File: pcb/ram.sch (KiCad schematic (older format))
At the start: 12 parts, among them J1 CONN_INTEGRALSTICK_FPGA_DEVICE, U2 XC7A50T-1FTG256C, U3 S27KS0641, U4 S27KS0641

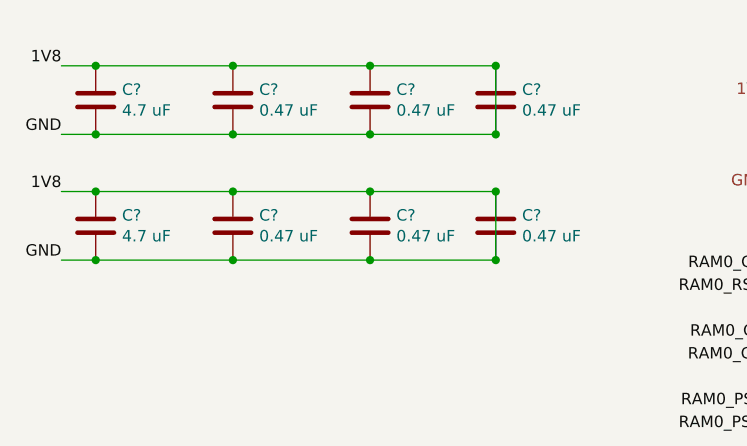
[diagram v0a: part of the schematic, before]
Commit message: Finished initial schematic. Pin assignments will likely change during routing. Ready for test point insertion and signoff review.
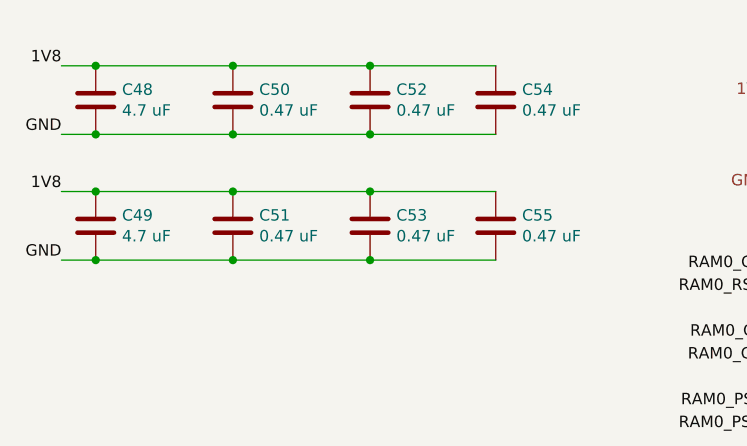
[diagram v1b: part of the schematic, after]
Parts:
- gave numbers to parts that had none: 8
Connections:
- net 1V8: no longer C48.2, C49.2, C50.2, C51.2, C52.2, C53.2, C54.2, C55.2, U3.B3 (VSS), U3.C1 (VSSQ), U3.E5 (VSSQ), U4.B3 (VSS), U4.C1 (VSSQ), U4.E5 (VSSQ)
- new net GND: C48.2, C49.2, C50.2, C51.2, C52.2, C53.2, C54.2, C55.2, U3.B3 (VSS), U3.C1 (VSSQ), U3.E5 (VSSQ), U4.B3 (VSS), U4.C1 (VSSQ), U4.E5 (VSSQ)
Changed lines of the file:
@@
 $Descr A4 11693 8268
 encoding utf-8
-Sheet 6 7
+Sheet 7 8
 Title "INTEGRALSTICK Compute Module"
-Date "2018-11-06"
+Date "2018-11-07"
 Rev "0.1"
 Comp "Andrew D. Zonenberg"
-Comment1 ""
+Comment1 "HyperRAM and 1.8V GPIO"
 Comment2 ""
 Comment3 ""
@@
 CLK_1V8_1
 $Comp
-L device:C C?
+L device:C C48
 U 1 1 5BF7E63E
 P 1000 950
-F 0 "C?" H 1115 996 50  0000 L CNN
+F 0 "C48" H 1115 996 50  0000 L CNN
 F 1 "4.7 uF" H 1115 905 50  0000 L CNN
 F 2 "" H 1038 800 50  0001 C CNN
@@
 $EndComp
 $Comp
-L device:C C?
+L device:C C50
 U 1 1 5BF7F429
 P 1600 950
-F 0 "C?" H 1715 996 50  0000 L CNN
+F 0 "C50" H 1715 996 50  0000 L CNN
 F 1 "0.47 uF" H 1715 905 50  0000 L CNN
 F 2 "" H 1638 800 50  0001 C CNN
@@
 $EndComp
 $Comp
-L device:C C?
+L device:C C52
 U 1 1 5BF7F82E
 P 2200 950
-F 0 "C?" H 2315 996 50  0000 L CNN
+F 0 "C52" H 2315 996 50  0000 L CNN
 F 1 "0.47 uF" H 2315 905 50  0000 L CNN
 F 2 "" H 2238 800 50  0001 C CNN
@@
 $EndComp
 $Comp
-L device:C C?
+L device:C C54
 U 1 1 5BF7FC5D
 P 2750 950
-F 0 "C?" H 2865 996 50  0000 L CNN
+F 0 "C54" H 2865 996 50  0000 L CNN
 F 1 "0.47 uF" H 2865 905 50  0000 L CNN
 F 2 "" H 2788 800 50  0001 C CNN
@@
 Wire Wire Line
 	850  1100 1000 1100
-Wire Wire Line
-	2750 1100 2750 800
-Connection ~ 2750 1100
 Connection ~ 1000 1100
 Wire Wire Line
@@
 Wire Wire Line
 	850  800  1000 800
-Connection ~ 2750 800
 Connection ~ 1000 800
 Wire Wire Line
@@
 	2200 800  2750 800
 $Comp
-L device:C C?
+L device:C C49
 U 1 1 5BF87471
 P 1000 1500
-F 0 "C?" H 1115 1546 50  0000 L CNN
+F 0 "C49" H 1115 1546 50  0000 L CNN
 F 1 "4.7 uF" H 1115 1455 50  0000 L CNN
 F 2 "" H 1038 1350 50  0001 C CNN
@@
 $EndComp
 $Comp
-L device:C C?
+L device:C C51
 U 1 1 5BF8747B
 P 1600 1500
-F 0 "C?" H 1715 1546 50  0000 L CNN
+F 0 "C51" H 1715 1546 50  0000 L CNN
 F 1 "0.47 uF" H 1715 1455 50  0000 L CNN
 F 2 "" H 1638 1350 50  0001 C CNN
@@
 $EndComp
 $Comp
-L device:C C?
+L device:C C53
 U 1 1 5BF87485
 P 2200 1500
-F 0 "C?" H 2315 1546 50  0000 L CNN
+F 0 "C53" H 2315 1546 50  0000 L CNN
 F 1 "0.47 uF" H 2315 1455 50  0000 L CNN
 F 2 "" H 2238 1350 50  0001 C CNN
@@
 $EndComp
 $Comp
-L device:C C?
+L device:C C55
 U 1 1 5BF8748F
 P 2750 1500
-F 0 "C?" H 2865 1546 50  0000 L CNN
+F 0 "C55" H 2865 1546 50  0000 L CNN
 F 1 "0.47 uF" H 2865 1455 50  0000 L CNN
 F 2 "" H 2788 1350 50  0001 C CNN
@@
 Wire Wire Line
 	850  1650 1000 1650
-Wire Wire Line
-	2750 1650 2750 1350
-Connection ~ 2750 1650
 Connection ~ 1000 1650
 Wire Wire Line
@@
 Wire Wire Line
 	850  1350 1000 1350
-Connection ~ 2750 1350
 Connection ~ 1000 1350
 Wire Wire Line

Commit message: Finished schematic signoff review. Fixed oscillator pinout bug, added some test points.
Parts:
- added TP11, TP12, TP13, TP14, TP15, TP16: SOLDERPROBE, symbol conn:CONN_01X01
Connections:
- net RAM0_CK_N: now also TP12.1 (P1)
- net RAM0_CK_P: now also TP11.1 (P1)
- net RAM0_DQ0: now also TP16.1 (P1)
- net RAM0_DQS: now also TP15.1 (P1)
- net RAM0_PSC_N: now also TP14.1 (P1)
- net RAM0_PSC_P: now also TP13.1 (P1)
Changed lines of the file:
@@
 Sheet 7 8
 Title "INTEGRALSTICK Compute Module"
-Date "2018-11-07"
+Date "2018-11-09"
 Rev "0.1"
 Comp "Andrew D. Zonenberg"
@@
 Wire Wire Line
 	2200 1350 2750 1350
+$Comp
+L conn:CONN_01X01 TP11
+U 1 1 5D407FEC
+P 1850 2350
+F 0 "TP11" H 1928 2391 50  0000 L CNN
+F 1 "SOLDERPROBE" H 1928 2300 50  0000 L CNN
+F 2 "" H 1850 2350 50  0001 C CNN
+F 3 "" H 1850 2350 50  0001 C CNN
+	1    1850 2350
+	1    0    0    -1
+$EndComp
+Text Label 1650 2350 2    50   ~ 0
+RAM0_CK_P
+$Comp
+L conn:CONN_01X01 TP12
+U 1 1 5D408C8E
+P 1850 2600
+F 0 "TP12" H 1928 2641 50  0000 L CNN
+F 1 "SOLDERPROBE" H 1928 2550 50  0000 L CNN
+F 2 "" H 1850 2600 50  0001 C CNN
+F 3 "" H 1850 2600 50  0001 C CNN
+	1    1850 2600
+	1    0    0    -1
+$EndComp
+Text Label 1650 2600 2    50   ~ 0
+RAM0_CK_N
+$Comp
+L conn:CONN_01X01 TP13
+U 1 1 5D40CFAA
+P 1850 2900
+F 0 "TP13" H 1928 2941 50  0000 L CNN
+F 1 "SOLDERPROBE" H 1928 2850 50  0000 L CNN
+F 2 "" H 1850 2900 50  0001 C CNN
+F 3 "" H 1850 2900 50  0001 C CNN
+	1    1850 2900
+	1    0    0    -1
+$EndComp
+Text Label 1650 2900 2    50   ~ 0
+RAM0_PSC_P
+$Comp
+L conn:CONN_01X01 TP14
+U 1 1 5D40CFB5
+P 1850 3150
+F 0 "TP14" H 1928 3191 50  0000 L CNN
+F 1 "SOLDERPROBE" H 1928 3100 50  0000 L CNN
+F 2 "" H 1850 3150 50  0001 C CNN
+F 3 "" H 1850 3150 50  0001 C CNN
+	1    1850 3150
+	1    0    0    -1
+$EndComp
+Text Label 1650 3150 2    50   ~ 0
+RAM0_PSC_N
+$Comp
+L conn:CONN_01X01 TP15
+U 1 1 5D40F583
+P 1850 3450
+F 0 "TP15" H 1928 3491 50  0000 L CNN
+F 1 "SOLDERPROBE" H 1928 3400 50  0000 L CNN
+F 2 "" H 1850 3450 50  0001 C CNN
+F 3 "" H 1850 3450 50  0001 C CNN
+	1    1850 3450
+	1    0    0    -1
+$EndComp
+Text Label 1650 3450 2    50   ~ 0
+RAM0_DQS
+$Comp
+L conn:CONN_01X01 TP16
+U 1 1 5D4115D3
+P 1850 3750
+F 0 "TP16" H 1928 3791 50  0000 L CNN
+F 1 "SOLDERPROBE" H 1928 3700 50  0000 L CNN
+F 2 "" H 1850 3750 50  0001 C CNN
+F 3 "" H 1850 3750 50  0001 C CNN
+	1    1850 3750
+	1    0    0    -1
+$EndComp
+Text Label 1650 3750 2    50   ~ 0
+RAM0_DQ0
 $EndSCHEMATC

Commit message: Assigned lots of footprints. Still have a few to go.
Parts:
- removed TP11, TP12, TP13, TP14, TP15, TP16: SOLDERPROBE, symbol conn:CONN_01X01
- C48, C49: footprint (none) -> azonenberg_pcb:EIA_0603_CAP_NOSILK
- C50, C51, C52, C53, C54, C55: footprint (none) -> azonenberg_pcb:EIA_0402_CAP_NOSILK
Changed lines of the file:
@@
 F 0 "C48" H 1115 996 50  0000 L CNN
 F 1 "4.7 uF" H 1115 905 50  0000 L CNN
-F 2 "" H 1038 800 50  0001 C CNN
+F 2 "azonenberg_pcb:EIA_0603_CAP_NOSILK" H 1038 800 50  0001 C CNN
 F 3 "" H 1000 950 50  0001 C CNN
 	1    1000 950
@@
 F 0 "C50" H 1715 996 50  0000 L CNN
 F 1 "0.47 uF" H 1715 905 50  0000 L CNN
-F 2 "" H 1638 800 50  0001 C CNN
+F 2 "azonenberg_pcb:EIA_0402_CAP_NOSILK" H 1638 800 50  0001 C CNN
 F 3 "" H 1600 950 50  0001 C CNN
 	1    1600 950
@@
 F 0 "C52" H 2315 996 50  0000 L CNN
 F 1 "0.47 uF" H 2315 905 50  0000 L CNN
-F 2 "" H 2238 800 50  0001 C CNN
+F 2 "azonenberg_pcb:EIA_0402_CAP_NOSILK" H 2238 800 50  0001 C CNN
 F 3 "" H 2200 950 50  0001 C CNN
 	1    2200 950
@@
 F 0 "C54" H 2865 996 50  0000 L CNN
 F 1 "0.47 uF" H 2865 905 50  0000 L CNN
-F 2 "" H 2788 800 50  0001 C CNN
+F 2 "azonenberg_pcb:EIA_0402_CAP_NOSILK" H 2788 800 50  0001 C CNN
 F 3 "" H 2750 950 50  0001 C CNN
 	1    2750 950
@@
 F 0 "C49" H 1115 1546 50  0000 L CNN
 F 1 "4.7 uF" H 1115 1455 50  0000 L CNN
-F 2 "" H 1038 1350 50  0001 C CNN
+F 2 "azonenberg_pcb:EIA_0603_CAP_NOSILK" H 1038 1350 50  0001 C CNN
 F 3 "" H 1000 1500 50  0001 C CNN
 	1    1000 1500
@@
 F 0 "C51" H 1715 1546 50  0000 L CNN
 F 1 "0.47 uF" H 1715 1455 50  0000 L CNN
-F 2 "" H 1638 1350 50  0001 C CNN
+F 2 "azonenberg_pcb:EIA_0402_CAP_NOSILK" H 1638 1350 50  0001 C CNN
 F 3 "" H 1600 1500 50  0001 C CNN
 	1    1600 1500
@@
 F 0 "C53" H 2315 1546 50  0000 L CNN
 F 1 "0.47 uF" H 2315 1455 50  0000 L CNN
-F 2 "" H 2238 1350 50  0001 C CNN
+F 2 "azonenberg_pcb:EIA_0402_CAP_NOSILK" H 2238 1350 50  0001 C CNN
 F 3 "" H 2200 1500 50  0001 C CNN
 	1    2200 1500
@@
 F 0 "C55" H 2865 1546 50  0000 L CNN
 F 1 "0.47 uF" H 2865 1455 50  0000 L CNN
-F 2 "" H 2788 1350 50  0001 C CNN
+F 2 "azonenberg_pcb:EIA_0402_CAP_NOSILK" H 2788 1350 50  0001 C CNN
 F 3 "" H 2750 1500 50  0001 C CNN
 	1    2750 1500
@@
 Wire Wire Line
 	2200 1350 2750 1350
-$Comp
-L conn:CONN_01X01 TP11
-U 1 1 5D407FEC
-P 1850 2350
-F 0 "TP11" H 1928 2391 50  0000 L CNN
-F 1 "SOLDERPROBE" H 1928 2300 50  0000 L CNN
-F 2 "" H 1850 2350 50  0001 C CNN
-F 3 "" H 1850 2350 50  0001 C CNN
-	1    1850 2350
-	1    0    0    -1
-$EndComp
-Text Label 1650 2350 2    50   ~ 0
-RAM0_CK_P
-$Comp
-L conn:CONN_01X01 TP12
-U 1 1 5D408C8E
-P 1850 2600
-F 0 "TP12" H 1928 2641 50  0000 L CNN
-F 1 "SOLDERPROBE" H 1928 2550 50  0000 L CNN
-F 2 "" H 1850 2600 50  0001 C CNN
-F 3 "" H 1850 2600 50  0001 C CNN
-	1    1850 2600
-	1    0    0    -1
-$EndComp
-Text Label 1650 2600 2    50   ~ 0
-RAM0_CK_N
-$Comp
-L conn:CONN_01X01 TP13
-U 1 1 5D40CFAA
-P 1850 2900
-F 0 "TP13" H 1928 2941 50  0000 L CNN
-F 1 "SOLDERPROBE" H 1928 2850 50  0000 L CNN
-F 2 "" H 1850 2900 50  0001 C CNN
-F 3 "" H 1850 2900 50  0001 C CNN
-	1    1850 2900
-	1    0    0    -1
-$EndComp
-Text Label 1650 2900 2    50   ~ 0
-RAM0_PSC_P
-$Comp
-L conn:CONN_01X01 TP14
-U 1 1 5D40CFB5
-P 1850 3150
-F 0 "TP14" H 1928 3191 50  0000 L CNN
-F 1 "SOLDERPROBE" H 1928 3100 50  0000 L CNN
-F 2 "" H 1850 3150 50  0001 C CNN
-F 3 "" H 1850 3150 50  0001 C CNN
-	1    1850 3150
-	1    0    0    -1
-$EndComp
-Text Label 1650 3150 2    50   ~ 0
-RAM0_PSC_N
-$Comp
-L conn:CONN_01X01 TP15
-U 1 1 5D40F583
-P 1850 3450
-F 0 "TP15" H 1928 3491 50  0000 L CNN
-F 1 "SOLDERPROBE" H 1928 3400 50  0000 L CNN
-F 2 "" H 1850 3450 50  0001 C CNN
-F 3 "" H 1850 3450 50  0001 C CNN
-	1    1850 3450
-	1    0    0    -1
-$EndComp
-Text Label 1650 3450 2    50   ~ 0
-RAM0_DQS
-$Comp
-L conn:CONN_01X01 TP16
-U 1 1 5D4115D3
-P 1850 3750
-F 0 "TP16" H 1928 3791 50  0000 L CNN
-F 1 "SOLDERPROBE" H 1928 3700 50  0000 L CNN
-F 2 "" H 1850 3750 50  0001 C CNN
-F 3 "" H 1850 3750 50  0001 C CNN
-	1    1850 3750
-	1    0    0    -1
-$EndComp
-Text Label 1650 3750 2    50   ~ 0
-RAM0_DQ0
 $EndSCHEMATC

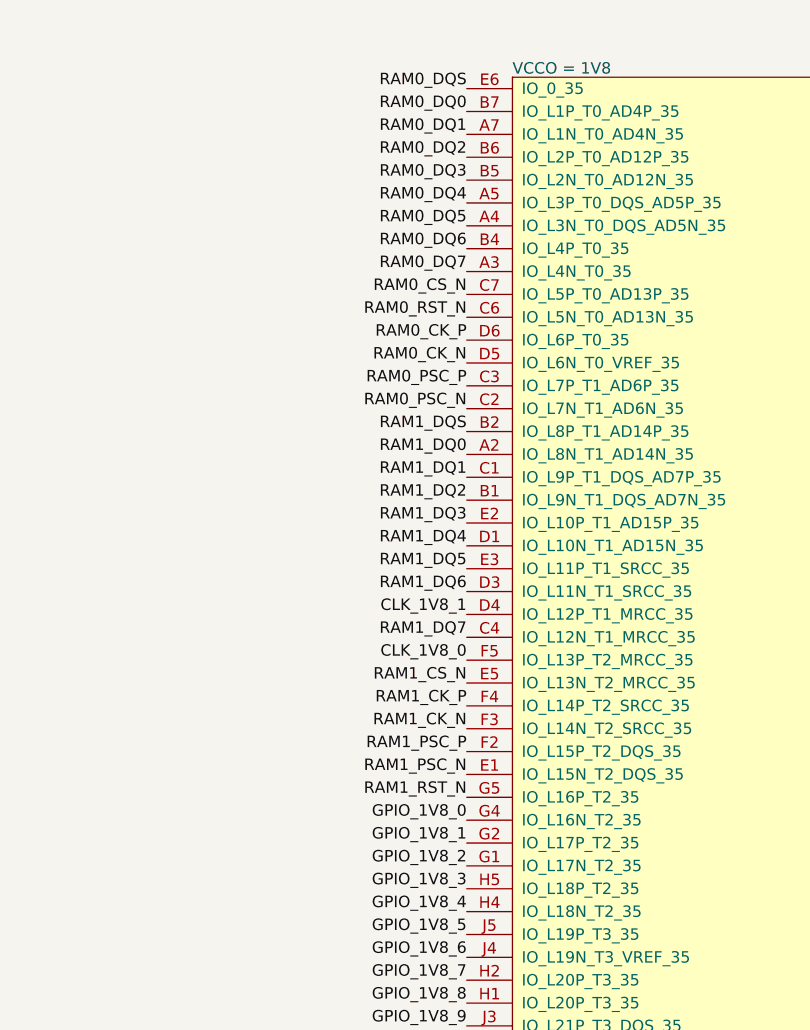
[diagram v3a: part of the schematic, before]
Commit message: Finished first iteration layout of RAM. Lots of pin swaps.
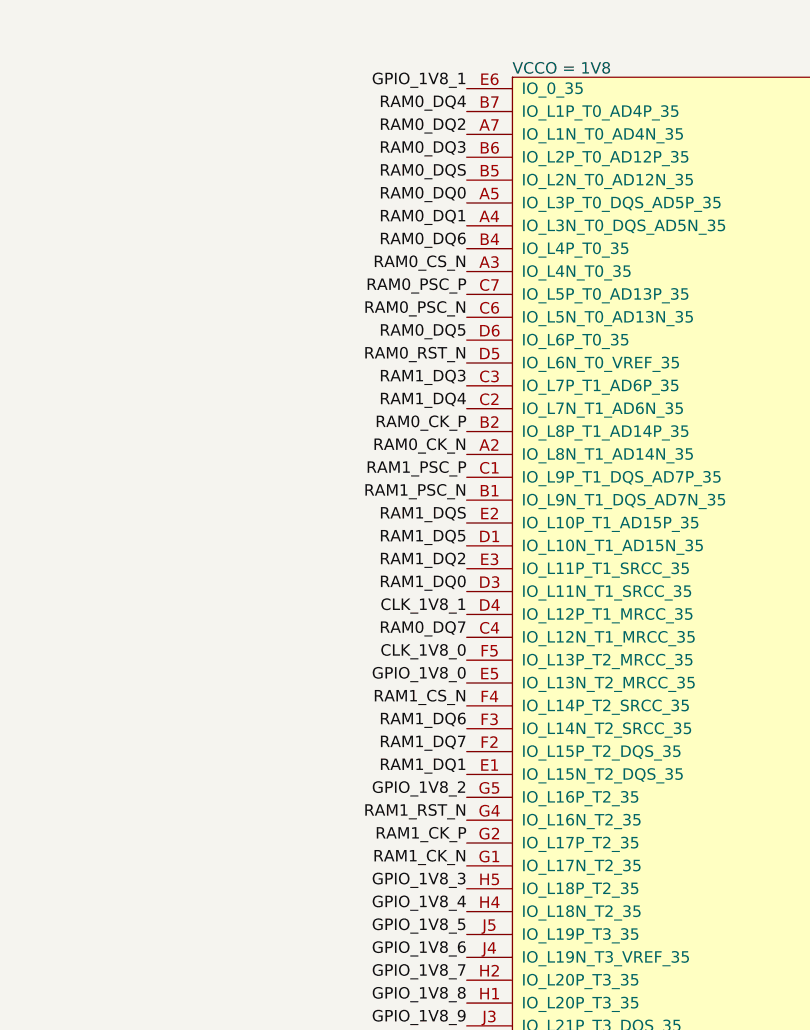
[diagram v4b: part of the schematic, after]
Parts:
- U2: footprint azonenberg_pcb:BGA_256_17x17_FULLARRAY_1MM -> azonenberg_pcb:BGA_256_17x17_FULLARRAY_1MM_0.4MM_FTG256
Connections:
- net GPIO_1V8_0: now also U2.E5 (IO_L13N_T2_MRCC_35); no longer U2.G4 (IO_L16N_T2_35)
- net GPIO_1V8_1: now also U2.E6 (IO_0_35); no longer U2.G2 (IO_L17P_T2_35)
- net GPIO_1V8_2: now also U2.G5 (IO_L16P_T2_35); no longer U2.G1 (IO_L17N_T2_35)
- net RAM0_CK_N: now also U2.A2 (IO_L8N_T1_AD14N_35); no longer U2.D5 (IO_L6N_T0_VREF_35)
- net RAM0_CK_P: now also U2.B2 (IO_L8P_T1_AD14P_35); no longer U2.D6 (IO_L6P_T0_35)
- net RAM0_CS_N: now also U2.A3 (IO_L4N_T0_35); no longer U2.C7 (IO_L5P_T0_AD13P_35)
- net RAM0_DQ0: now also U2.A5 (IO_L3P_T0_DQS_AD5P_35); no longer U2.B7 (IO_L1P_T0_AD4P_35)
- net RAM0_DQ1: now also U2.A4 (IO_L3N_T0_DQS_AD5N_35); no longer U2.A7 (IO_L1N_T0_AD4N_35)
- net RAM0_DQ2: now also U2.A7 (IO_L1N_T0_AD4N_35); no longer U2.B6 (IO_L2P_T0_AD12P_35)
- net RAM0_DQ3: now also U2.B6 (IO_L2P_T0_AD12P_35); no longer U2.B5 (IO_L2N_T0_AD12N_35)
- net RAM0_DQ4: now also U2.B7 (IO_L1P_T0_AD4P_35); no longer U2.A5 (IO_L3P_T0_DQS_AD5P_35)
- net RAM0_DQ5: now also U2.D6 (IO_L6P_T0_35); no longer U2.A4 (IO_L3N_T0_DQS_AD5N_35)
- net RAM0_DQ7: now also U2.C4 (IO_L12N_T1_MRCC_35); no longer U2.A3 (IO_L4N_T0_35)
- net RAM0_DQS: now also U2.B5 (IO_L2N_T0_AD12N_35); no longer U2.E6 (IO_0_35)
- net RAM0_PSC_N: now also U2.C6 (IO_L5N_T0_AD13N_35); no longer U2.C2 (IO_L7N_T1_AD6N_35)
- net RAM0_PSC_P: now also U2.C7 (IO_L5P_T0_AD13P_35); no longer U2.C3 (IO_L7P_T1_AD6P_35)
- net RAM0_RST_N: now also U2.D5 (IO_L6N_T0_VREF_35); no longer U2.C6 (IO_L5N_T0_AD13N_35)
- net RAM1_CK_N: now also U2.G1 (IO_L17N_T2_35); no longer U2.F3 (IO_L14N_T2_SRCC_35)
- net RAM1_CK_P: now also U2.G2 (IO_L17P_T2_35); no longer U2.F4 (IO_L14P_T2_SRCC_35)
- net RAM1_CS_N: now also U2.F4 (IO_L14P_T2_SRCC_35); no longer U2.E5 (IO_L13N_T2_MRCC_35)
- net RAM1_DQ0: now also U2.D3 (IO_L11N_T1_SRCC_35); no longer U2.A2 (IO_L8N_T1_AD14N_35)
- net RAM1_DQ1: now also U2.E1 (IO_L15N_T2_DQS_35); no longer U2.C1 (IO_L9P_T1_DQS_AD7P_35)
- net RAM1_DQ2: now also U2.E3 (IO_L11P_T1_SRCC_35); no longer U2.B1 (IO_L9N_T1_DQS_AD7N_35)
- net RAM1_DQ3: now also U2.C3 (IO_L7P_T1_AD6P_35); no longer U2.E2 (IO_L10P_T1_AD15P_35)
- net RAM1_DQ4: now also U2.C2 (IO_L7N_T1_AD6N_35); no longer U2.D1 (IO_L10N_T1_AD15N_35)
- net RAM1_DQ5: now also U2.D1 (IO_L10N_T1_AD15N_35); no longer U2.E3 (IO_L11P_T1_SRCC_35)
- net RAM1_DQ6: now also U2.F3 (IO_L14N_T2_SRCC_35); no longer U2.D3 (IO_L11N_T1_SRCC_35)
- net RAM1_DQ7: now also U2.F2 (IO_L15P_T2_DQS_35); no longer U2.C4 (IO_L12N_T1_MRCC_35)
- net RAM1_DQS: now also U2.E2 (IO_L10P_T1_AD15P_35); no longer U2.B2 (IO_L8P_T1_AD14P_35)
- net RAM1_PSC_N: now also U2.B1 (IO_L9N_T1_DQS_AD7N_35); no longer U2.E1 (IO_L15N_T2_DQS_35)
- net RAM1_PSC_P: now also U2.C1 (IO_L9P_T1_DQS_AD7P_35); no longer U2.F2 (IO_L15P_T2_DQS_35)
- net RAM1_RST_N: now also U2.G4 (IO_L16N_T2_35); no longer U2.G5 (IO_L16P_T2_35)
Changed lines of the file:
@@
 Sheet 7 8
 Title "INTEGRALSTICK Compute Module"
-Date "2018-11-09"
+Date "2018-11-11"
 Rev "0.1"
 Comp "Andrew D. Zonenberg"
@@
 F 0 "U2" H 10177 8308 60  0000 L CNN
 F 1 "XC7A50T-1FTG256C" H 10177 8202 60  0000 L CNN
-F 2 "azonenberg_pcb:BGA_256_17x17_FULLARRAY_1MM" H 8800 5800 60  0001 C CNN
+F 2 "azonenberg_pcb:BGA_256_17x17_FULLARRAY_1MM_0.4MM_FTG256" H 8800 5800 60  0001 C CNN
 F 3 "" H 8800 5800 60  0000 C CNN
 	6    8800 5800
@@
 Wire Wire Line
 	5500 1800 5600 1800
-Text Label 8600 900  2    50   ~ 0
+Text Label 8600 1300 2    50   ~ 0
 RAM0_DQS
+Text Label 8600 1400 2    50   ~ 0
+RAM0_DQ0
+Text Label 8600 1500 2    50   ~ 0
+RAM0_DQ1
+Text Label 8600 1100 2    50   ~ 0
+RAM0_DQ2
+Text Label 8600 1200 2    50   ~ 0
+RAM0_DQ3
 Text Label 8600 1000 2    50   ~ 0
-RAM0_DQ0
-Text Label 8600 1100 2    50   ~ 0
-RAM0_DQ1
-Text Label 8600 1200 2    50   ~ 0
-RAM0_DQ2
-Text Label 8600 1300 2    50   ~ 0
-RAM0_DQ3
-Text Label 8600 1400 2    50   ~ 0
 RAM0_DQ4
-Text Label 8600 1500 2    50   ~ 0
+Text Label 8600 2000 2    50   ~ 0
 RAM0_DQ5
 Text Label 8600 1600 2    50   ~ 0
 RAM0_DQ6
+Text Label 8600 3300 2    50   ~ 0
+RAM0_DQ7
+Text Label 8600 2100 2    50   ~ 0
+RAM0_RST_N
 Text Label 8600 1700 2    50   ~ 0
-RAM0_DQ7
+RAM0_CS_N
+Text Label 8600 2400 2    50   ~ 0
+RAM0_CK_P
+Text Label 8600 2500 2    50   ~ 0
+RAM0_CK_N
+Text Label 8600 1800 2    50   ~ 0
+RAM0_PSC_P
 Text Label 8600 1900 2    50   ~ 0
-RAM0_RST_N
-Text Label 8600 1800 2    50   ~ 0
-RAM0_CS_N
-Text Label 8600 2000 2    50   ~ 0
-RAM0_CK_P
-Text Label 8600 2100 2    50   ~ 0
-RAM0_CK_N
+RAM0_PSC_N
+Text Label 8600 2800 2    50   ~ 0
+RAM1_DQS
+Text Label 8600 3100 2    50   ~ 0
+RAM1_DQ0
+Text Label 8600 3900 2    50   ~ 0
+RAM1_DQ1
+Text Label 8600 3000 2    50   ~ 0
+RAM1_DQ2
 Text Label 8600 2200 2    50   ~ 0
-RAM0_PSC_P
+RAM1_DQ3
 Text Label 8600 2300 2    50   ~ 0
-RAM0_PSC_N
-Text Label 8600 2400 2    50   ~ 0
-RAM1_DQS
-Text Label 8600 2500 2    50   ~ 0
-RAM1_DQ0
+RAM1_DQ4
+Text Label 8600 2900 2    50   ~ 0
+RAM1_DQ5
+Text Label 8600 3700 2    50   ~ 0
+RAM1_DQ6
+Text Label 8600 3800 2    50   ~ 0
+RAM1_DQ7
+Text Label 8600 4100 2    50   ~ 0
+RAM1_RST_N
+Text Label 8600 3600 2    50   ~ 0
+RAM1_CS_N
+Text Label 8600 4200 2    50   ~ 0
+RAM1_CK_P
+Text Label 8600 4300 2    50   ~ 0
+RAM1_CK_N
 Text Label 8600 2600 2    50   ~ 0
-RAM1_DQ1
+RAM1_PSC_P
 Text Label 8600 2700 2    50   ~ 0
-RAM1_DQ2
-Text Label 8600 2800 2    50   ~ 0
-RAM1_DQ3
-Text Label 8600 2900 2    50   ~ 0
-RAM1_DQ4
-Text Label 8600 3000 2    50   ~ 0
-RAM1_DQ5
-Text Label 8600 3100 2    50   ~ 0
-RAM1_DQ6
-Text Label 8600 3300 2    50   ~ 0
-RAM1_DQ7
-Text Label 8600 4000 2    50   ~ 0
-RAM1_RST_N
-Text Label 8600 3500 2    50   ~ 0
-RAM1_CS_N
-Text Label 8600 3600 2    50   ~ 0
-RAM1_CK_P
-Text Label 8600 3700 2    50   ~ 0
-RAM1_CK_N
-Text Label 8600 3800 2    50   ~ 0
-RAM1_PSC_P
-Text Label 8600 3900 2    50   ~ 0
 RAM1_PSC_N
 $Comp
@@
 	-1   0    0    -1
 $EndComp
-Text Label 8600 4100 2    50   ~ 0
+Text Label 8600 3500 2    50   ~ 0
 GPIO_1V8_0
-Text Label 8600 4200 2    50   ~ 0
+Text Label 8600 900  2    50   ~ 0
 GPIO_1V8_1
-Text Label 8600 4300 2    50   ~ 0
+Text Label 8600 4000 2    50   ~ 0
 GPIO_1V8_2
 Text Label 8600 4400 2    50   ~ 0

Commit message: More efficient use of top right area above FPGA
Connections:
- net GPIO_1V8_0: now also U2.J3 (IO_L21P_T3_DQS_35); no longer U2.E5 (IO_L13N_T2_MRCC_35)
- net GPIO_1V8_1: now also U2.H2 (IO_L20P_T3_35); no longer U2.E6 (IO_0_35)
- net GPIO_1V8_10: now also U2.J5 (IO_L19P_T3_35); no longer U2.H3 (IO_L21P_T3_DQS_35)
- net GPIO_1V8_12: now also U2.G5 (IO_L16P_T2_35); no longer U2.J1 (IO_L22N_T3_35)
- net GPIO_1V8_15: now also U2.H4 (IO_L18N_T2_35); no longer U2.K3 (IO_L24P_T3_35)
- net GPIO_1V8_2: now also U2.J1 (IO_L22N_T3_35); no longer U2.G5 (IO_L16P_T2_35)
- net GPIO_1V8_3: now also U2.H1 (IO_L20P_T3_35); no longer U2.H5 (IO_L18P_T2_35)
- net GPIO_1V8_4: now also U2.K3 (IO_L24P_T3_35); no longer U2.H4 (IO_L18N_T2_35)
- net GPIO_1V8_5: now also U2.H3 (IO_L21P_T3_DQS_35); no longer U2.J5 (IO_L19P_T3_35)
- net GPIO_1V8_7: now also U2.E6 (IO_0_35); no longer U2.H2 (IO_L20P_T3_35)
- net GPIO_1V8_8: now also U2.H5 (IO_L18P_T2_35); no longer U2.H1 (IO_L20P_T3_35)
- net GPIO_1V8_9: now also U2.E5 (IO_L13N_T2_MRCC_35); no longer U2.J3 (IO_L21P_T3_DQS_35)
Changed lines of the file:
@@
 	-1   0    0    -1
 $EndComp
-Text Label 8600 3500 2    50   ~ 0
+Text Label 8600 5000 2    50   ~ 0
 GPIO_1V8_0
-Text Label 8600 900  2    50   ~ 0
+Text Label 8600 4800 2    50   ~ 0
 GPIO_1V8_1
-Text Label 8600 4000 2    50   ~ 0
+Text Label 8600 5300 2    50   ~ 0
 GPIO_1V8_2
-Text Label 8600 4400 2    50   ~ 0
+Text Label 8600 4900 2    50   ~ 0
 GPIO_1V8_3
-Text Label 8600 4500 2    50   ~ 0
+Text Label 8600 5600 2    50   ~ 0
 GPIO_1V8_4
-Text Label 8600 4600 2    50   ~ 0
+Text Label 8600 5100 2    50   ~ 0
 GPIO_1V8_5
 Text Label 8600 4700 2    50   ~ 0
 GPIO_1V8_6
-Text Label 8600 4800 2    50   ~ 0
+Text Label 8600 900  2    50   ~ 0
 GPIO_1V8_7
-Text Label 8600 4900 2    50   ~ 0
+Text Label 8600 4400 2    50   ~ 0
 GPIO_1V8_8
-Text Label 8600 5000 2    50   ~ 0
+Text Label 8600 3500 2    50   ~ 0
 GPIO_1V8_9
-Text Label 8600 5100 2    50   ~ 0
+Text Label 8600 4600 2    50   ~ 0
 GPIO_1V8_10
 Text Label 8600 5200 2    50   ~ 0
 GPIO_1V8_11
-Text Label 8600 5300 2    50   ~ 0
+Text Label 8600 4000 2    50   ~ 0
 GPIO_1V8_12
 Text Label 8600 5400 2    50   ~ 0
@@
 Text Label 8600 5500 2    50   ~ 0
 GPIO_1V8_14
-Text Label 8600 5600 2    50   ~ 0
+Text Label 8600 4500 2    50   ~ 0
 GPIO_1V8_15
 Text Label 8600 5700 2    50   ~ 0
